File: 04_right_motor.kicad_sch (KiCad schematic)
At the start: 9 parts, among them J5 RIGHT MOTOR + ENCODER, U3 VNH5019A-E

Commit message: Correct motor cable pinout and add power solder pads
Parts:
- added J16: RIGHT MOTOR LARGE SOLDER PADS, Connector_Wire:SolderWire-1.5sqmm_1x02_P7.8mm_D1.7mm_OD3.9mm, symbol Connector_Generic:Conn_01x02
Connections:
- net 3V3: now also J5.5 (Pin_5); no longer J5.4 (Pin_4)
- net GND: now also J5.2 (Pin_2); no longer J5.3 (Pin_3)
- net RIGHT_ENC_A_RAW: now also J5.3 (Pin_3); no longer J5.5 (Pin_5)
- net RIGHT_ENC_B_RAW: now also J5.4 (Pin_4); no longer J5.6 (Pin_6)
- net RIGHT_OUTA: now also J16.1 (Pin_1)
- net RIGHT_OUTB: now also J5.6 (Pin_6), J16.2 (Pin_2); no longer J5.2 (Pin_2)
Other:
- note added: "J16: large 1.7 mm through-holes in parallel with pins 1/6 for separately soldered red and white motor-power wires."
- note added: "J4/J5 cable: 1 RED motor+; 2 BLACK encoder GND; 3 YELLOW encoder A; 4 GREEN encoder B; 5 BLUE encoder +3V3; 6 WHITE motor-."
- note removed: "J connector pinout: 1 red motor A; 2 white motor B; 3 black GND; 4 blue +3V3; 5 yellow encoder A; 6 green encoder B."

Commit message: Complete pre-PCB electrical and safety audit
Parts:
- added C16: 100 nF 50 V, Capacitor_SMD:C_0805_2012Metric, symbol Device:C
- added C17: 1 uF 25 V, Capacitor_SMD:C_0805_2012Metric, symbol Device:C
- added C19: 100 nF 50 V FIT AT MOTOR, symbol Device:C
- added D19, D20: BAT54, Diode_SMD:D_SOD-323, symbol Device:D_Schottky
- added F6: 5 A MINI BLADE MOTOR BRANCH, Fuse:Fuseholder_Blade_Mini_Keystone_3568, symbol Device:Fuse
- added R94, R95: 10 k pulldown, Resistor_SMD:R_0805_2012Metric, symbol Device:R
- added R96: 10 k fault pullup, Resistor_SMD:R_0805_2012Metric, symbol Device:R
- added R98: 4.7 k ADC protect, Resistor_SMD:R_0805_2012Metric, symbol Device:R
- added R99: 1 k diag series, Resistor_SMD:R_0805_2012Metric, symbol Device:R
- added TP30: VBAT, TestPoint:TestPoint_Loop_D2.50mm_Drill1.0mm, symbol Connector:TestPoint
- added TP31: PWM, TestPoint:TestPoint_Loop_D2.50mm_Drill1.0mm, symbol Connector:TestPoint
- added TP32: INA, TestPoint:TestPoint_Loop_D2.50mm_Drill1.0mm, symbol Connector:TestPoint
- added TP33: INB, TestPoint:TestPoint_Loop_D2.50mm_Drill1.0mm, symbol Connector:TestPoint
- added TP34: DIAG, TestPoint:TestPoint_Loop_D2.50mm_Drill1.0mm, symbol Connector:TestPoint
- added TP35: CS ADC, TestPoint:TestPoint_Loop_D2.50mm_Drill1.0mm, symbol Connector:TestPoint
- added TP36: ENC A, TestPoint:TestPoint_Loop_D2.50mm_Drill1.0mm, symbol Connector:TestPoint
- added TP37: ENC B, TestPoint:TestPoint_Loop_D2.50mm_Drill1.0mm, symbol Connector:TestPoint
- added TP38: GND, TestPoint:TestPoint_Loop_D2.50mm_Drill1.0mm, symbol Connector:TestPoint
- C15: value 470 uF 25 V -> 470 uF 35 V LOW ESR
- R14: value 1 k current sense -> 680 R current sense
- R90, R91, R92: value 100 k pulldown -> 1 k series
- R93: value 10 k fault pullup -> 10 k pulldown
- U3: footprint Package_SO:ST_MultiPowerSO-30 -> PickleballRobot:VNH5019_MultiPowerSO30_ThermalVias
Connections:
- net 3V3: now also D20.2 (A), R96.2; no longer J5.5 (Pin_5), R93.2
- net GND: now also R93.2, C16.2, C17.2, D19.1 (K), R94.2, R95.2, TP38.1; no longer R90.2, R91.2, R92.2
- net GPIO13_R_INA: no longer U3.4 (INA)
- net GPIO14_R_PWM: no longer U3.7 (PWM)
- net GPIO4_R_INB: no longer U3.10 (INB)
- net RIGHT_OUTA: now also C19.1
- net RIGHT_OUTB: now also C19.2
- net SENSOR_VN_GPIO39: now also D19.2 (A), D20.1 (K), R98.2, TP35.1; no longer R14.1, U3.8 (CS)
- net MOTOR_DIAG renamed RIGHT_DIAG
- net RIGHT_DIAG: now also R96.1, R99.1, TP34.1; no longer R93.1
- net RIGHT_ENC_A_RAW renamed RIGHT_ENC_A_CABLE
- net RIGHT_ENC_A_CABLE: now also TP36.1
- net RIGHT_ENC_B_RAW renamed RIGHT_ENC_B_CABLE
- net RIGHT_ENC_B_CABLE: now also TP37.1
- net VBAT_SW renamed RIGHT_VBAT
- net RIGHT_VBAT: now also C16.1, C17.1, F6.2, TP30.1
- new net ACT_VBAT: F6.1
- new net ENC_3V3: J5.5 (Pin_5)
- new net GPIO5_RIGHT_DIAG: R99.2
- new net RIGHT_CS_RAW: R14.1, R98.1, U3.8 (CS)
- new net RIGHT_INA_DRV: R91.2, R94.1, TP32.1, U3.4 (INA)
- new net RIGHT_INB_DRV: R92.2, R95.1, TP33.1, U3.10 (INB)
- new net RIGHT_PWM_DRV: R90.2, R93.1, TP31.1, U3.7 (PWM)

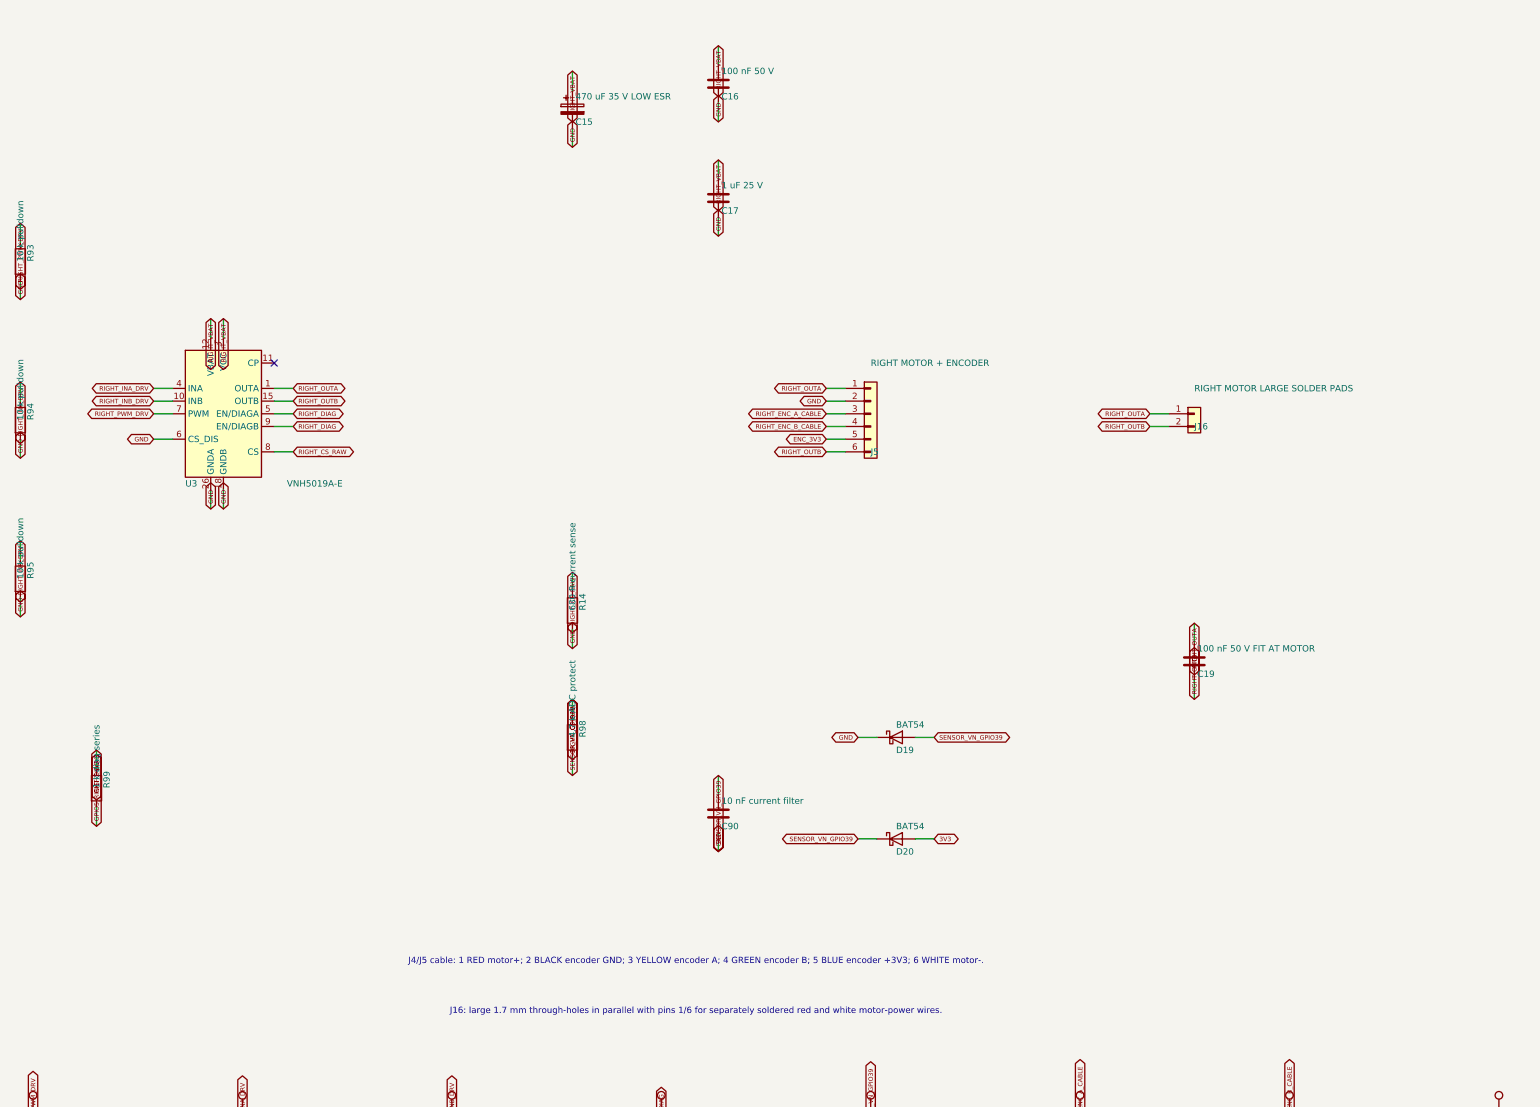
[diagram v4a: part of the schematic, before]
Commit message: Correct critical controller schematic safety issues
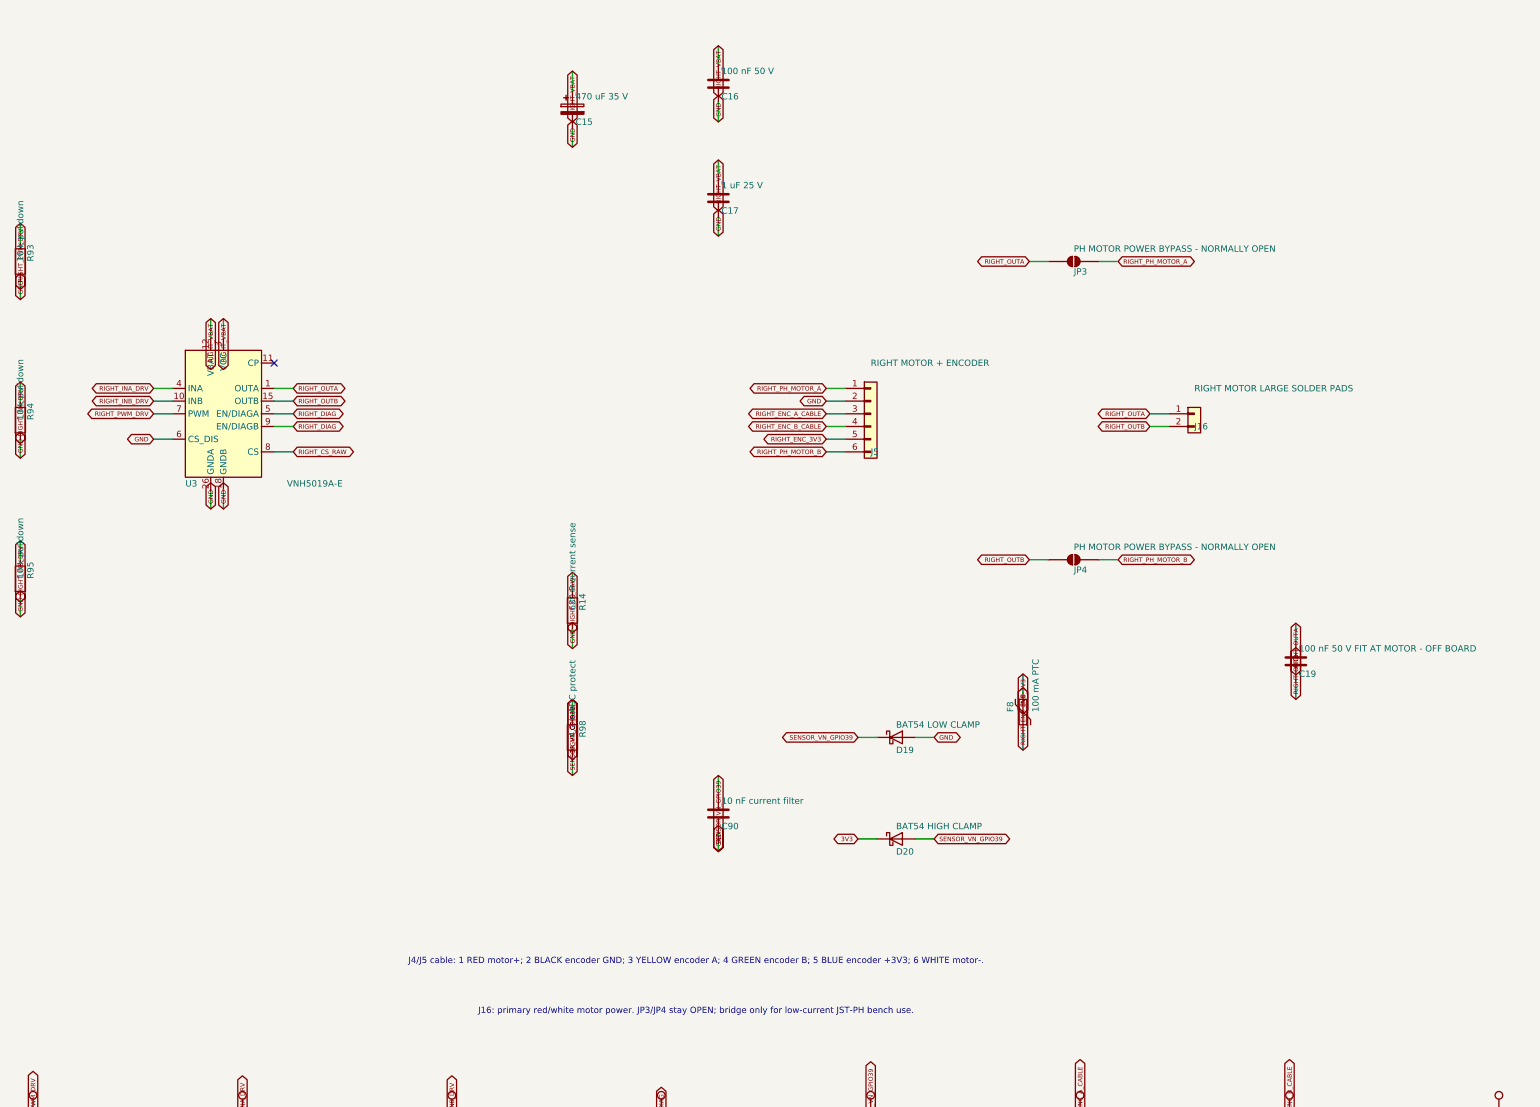
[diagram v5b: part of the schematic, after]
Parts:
- removed R99: 1 k diag series, Resistor_SMD:R_0805_2012Metric, symbol Device:R
- added F8: 100 mA PTC, Fuse:Fuse_0805_2012Metric, symbol Device:Polyfuse
- added JP3, JP4: PH MOTOR POWER BYPASS - NORMALLY OPEN, Jumper:SolderJumper-2_P1.3mm_Open_Pad1.0x1.5mm, symbol Jumper:SolderJumper_2_Open
- C15: value 470 uF 35 V LOW ESR -> 470 uF 35 V; footprint Capacitor_THT:CP_Radial_D8.0mm_P3.50mm -> Capacitor_THT:CP_Radial_D10.0mm_P5.00mm
- C19: value 100 nF 50 V FIT AT MOTOR -> 100 nF 50 V FIT AT MOTOR - OFF BOARD
- D19: value BAT54 -> BAT54 LOW CLAMP
- D20: value BAT54 -> BAT54 HIGH CLAMP
- TP30, TP31, TP32, TP33, TP34, TP35, TP36, TP37, TP38: footprint TestPoint:TestPoint_Loop_D2.50mm_Drill1.0mm -> TestPoint:TestPoint_Pad_D1.5mm; now left out of the parts list
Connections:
- net 3V3: now also D20.1 (K); no longer D20.2 (A)
- net ENC_3V3: now also F8.1; no longer J5.5 (Pin_5)
- net GND: now also D19.2 (A); no longer D19.1 (K)
- net RIGHT_OUTA: now also JP3.1 (A); no longer J5.1 (Pin_1)
- net RIGHT_OUTB: now also JP4.1 (A); no longer J5.6 (Pin_6)
- net SENSOR_VN_GPIO39: now also D19.1 (K), D20.2 (A); no longer D19.2 (A), D20.1 (K)
- new net RIGHT_ENC_3V3: F8.2, J5.5 (Pin_5)
- new net RIGHT_PH_MOTOR_A: J5.1 (Pin_1), JP3.2 (B)
- new net RIGHT_PH_MOTOR_B: J5.6 (Pin_6), JP4.2 (B)
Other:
- note added: "J16: primary red/white motor power. JP3/JP4 stay OPEN; bridge only for low-current JST-PH bench use."
- note removed: "J16: large 1.7 mm through-holes in parallel with pins 1/6 for separately soldered red and white motor-power wires."
